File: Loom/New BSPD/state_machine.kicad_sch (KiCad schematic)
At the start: 13 parts, among them U1 4011, U11 4012, U12 74LS573, U3 4011, U4 4011, U5 4011, U6 4011, U7 4011, U8 4011

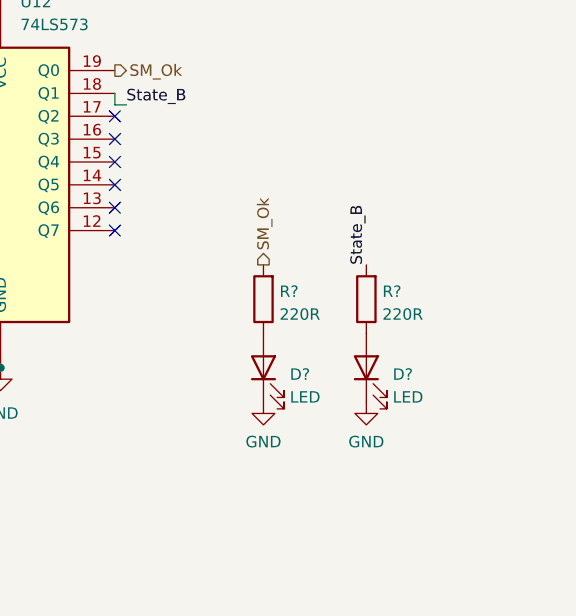
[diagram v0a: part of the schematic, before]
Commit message: Add test points
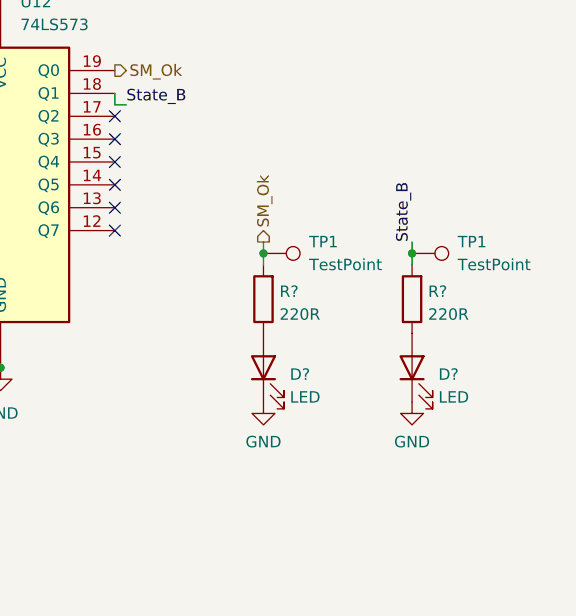
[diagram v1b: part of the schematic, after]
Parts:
- added TP1 (x2): TestPoint, TestPoint:TestPoint_THTPad_D3.0mm_Drill1.5mm, symbol Connector:TestPoint
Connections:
- net SM_Ok: now also TP1.1
- net State_B: now also TP1.1
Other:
- moved on the sheet: D?, R?
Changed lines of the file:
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@@
   (junction (at 171.45 22.86) (diameter 0) (color 0 0 0 0)
   )
+  (junction (at 252.73 71.12) (diameter 0) (color 0 0 0 0)
+  )
   (junction (at 158.75 55.88) (diameter 0) (color 0 0 0 0)
+  )
+  (junction (at 269.24 71.12) (diameter 0) (color 0 0 0 0)
   )
   (junction (at 223.52 83.82) (diameter 0) (color 0 0 0 0)
@@
     (stroke (width 0) (type default))
   )
+  (wire (pts (xy 252.73 71.12) (xy 252.73 72.39))
+    (stroke (width 0) (type default))
+  )
   (wire (pts (xy 109.22 74.93) (xy 113.03 74.93))
     (stroke (width 0) (type default))
@@
     (stroke (width 0) (type default))
   )
+  (wire (pts (xy 269.24 69.85) (xy 269.24 71.12))
+    (stroke (width 0) (type default))
+  )
   (wire (pts (xy 129.54 46.99) (xy 135.89 46.99))
     (stroke (width 0) (type default))
@@
     (stroke (width 0) (type default))
   )
+  (wire (pts (xy 252.73 69.85) (xy 252.73 71.12))
+    (stroke (width 0) (type default))
+  )
   (wire (pts (xy 158.75 30.48) (xy 158.75 43.18))
     (stroke (width 0) (type default))
@@
   )
   (wire (pts (xy 92.71 72.39) (xy 92.71 77.47))
+    (stroke (width 0) (type default))
+  )
+  (wire (pts (xy 269.24 71.12) (xy 269.24 72.39))
     (stroke (width 0) (type default))
   )
@@
     (effects (font (size 1.27 1.27)) (justify right bottom))
   )
-  (label "State_B" (at 264.16 72.39 90) (fields_autoplaced)
+  (label "State_B" (at 269.24 69.85 90) (fields_autoplaced)
     (effects (font (size 1.27 1.27)) (justify left bottom))
   )
@@
     (effects (font (size 1.27 1.27)) (justify right))
   )
-  (hierarchical_label "SM_Ok" (shape output) (at 252.73 72.39 90) (fields_autoplaced)
+  (hierarchical_label "SM_Ok" (shape output) (at 252.73 69.85 90) (fields_autoplaced)
     (effects (font (size 1.27 1.27)) (justify left))
   )
@@
     )
   )
-  (symbol (lib_id "Device:LED") (at 264.16 83.82 90) (unit 1)
-    (in_bom yes) (on_board yes) (dnp no) (fields_autoplaced)
-    (property "Reference" "D?" (at 267.081 84.5728 90)
+  (symbol (lib_id "Device:LED") (at 269.24 83.82 90) (unit 1)
+    (in_bom yes) (on_board yes) (dnp no) (fields_autoplaced)
+    (property "Reference" "D?" (at 272.161 84.5728 90)
       (effects (font (size 1.27 1.27)) (justify right))
     )
-    (property "Value" "LED" (at 267.081 87.1097 90)
+    (property "Value" "LED" (at 272.161 87.1097 90)
       (effects (font (size 1.27 1.27)) (justify right))
     )
-    (property "Footprint" "LED_THT:LED_D5.0mm" (at 264.16 83.82 0)
-      (effects (font (size 1.27 1.27)) hide)
-    )
-    (property "Datasheet" "~" (at 264.16 83.82 0)
+    (property "Footprint" "LED_THT:LED_D5.0mm" (at 269.24 83.82 0)
+      (effects (font (size 1.27 1.27)) hide)
+    )
+    (property "Datasheet" "~" (at 269.24 83.82 0)
       (effects (font (size 1.27 1.27)) hide)
     )
@@
     )
   )
-  (symbol (lib_id "Device:R") (at 264.16 76.2 180) (unit 1)
-    (in_bom yes) (on_board yes) (dnp no) (fields_autoplaced)
-    (property "Reference" "R?" (at 265.938 75.3653 0)
+  (symbol (lib_id "Device:R") (at 269.24 76.2 180) (unit 1)
+    (in_bom yes) (on_board yes) (dnp no) (fields_autoplaced)
+    (property "Reference" "R?" (at 271.018 75.3653 0)
       (effects (font (size 1.27 1.27)) (justify right))
     )
-    (property "Value" "220R" (at 265.938 77.9022 0)
+    (property "Value" "220R" (at 271.018 77.9022 0)
       (effects (font (size 1.27 1.27)) (justify right))
     )
-    (property "Footprint" "Resistor_THT:R_Axial_DIN0207_L6.3mm_D2.5mm_P7.62mm_Horizontal" (at 265.938 76.2 90)
-      (effects (font (size 1.27 1.27)) hide)
-    )
-    (property "Datasheet" "~" (at 264.16 76.2 0)
+    (property "Footprint" "Resistor_THT:R_Axial_DIN0207_L6.3mm_D2.5mm_P7.62mm_Horizontal" (at 271.018 76.2 90)
+      (effects (font (size 1.27 1.27)) hide)
+    )
+    (property "Datasheet" "~" (at 269.24 76.2 0)
       (effects (font (size 1.27 1.27)) hide)
     )
@@
     )
   )
-  (symbol (lib_id "power:GND") (at 264.16 87.63 0) (unit 1)
-    (in_bom yes) (on_board yes) (dnp no) (fields_autoplaced)
-    (property "Reference" "#PWR?" (at 264.16 93.98 0)
-      (effects (font (size 1.27 1.27)) hide)
-    )
-    (property "Value" "GND" (at 264.16 92.0734 0)
-      (effects (font (size 1.27 1.27)))
-    )
-    (property "Footprint" "" (at 264.16 87.63 0)
-      (effects (font (size 1.27 1.27)) hide)
-    )
-    (property "Datasheet" "" (at 264.16 87.63 0)
+  (symbol (lib_id "power:GND") (at 269.24 87.63 0) (unit 1)
+    (in_bom yes) (on_board yes) (dnp no) (fields_autoplaced)
+    (property "Reference" "#PWR?" (at 269.24 93.98 0)
+      (effects (font (size 1.27 1.27)) hide)
+    )
+    (property "Value" "GND" (at 269.24 92.0734 0)
+      (effects (font (size 1.27 1.27)))
+    )
+    (property "Footprint" "" (at 269.24 87.63 0)
+      (effects (font (size 1.27 1.27)) hide)
+    )
+    (property "Datasheet" "" (at 269.24 87.63 0)
       (effects (font (size 1.27 1.27)) hide)
     )
@@
     )
   )
+  (symbol (lib_id "Connector:TestPoint") (at 252.73 71.12 270) (unit 1)
+    (in_bom yes) (on_board yes) (dnp no) (fields_autoplaced)
+    (property "Reference" "TP1" (at 257.81 69.85 90)
+      (effects (font (size 1.27 1.27)) (justify left))
+    )
+    (property "Value" "TestPoint" (at 257.81 72.39 90)
+      (effects (font (size 1.27 1.27)) (justify left))
+    )
+    (property "Footprint" "TestPoint:TestPoint_THTPad_D3.0mm_Drill1.5mm" (at 252.73 76.2 0)
+      (effects (font (size 1.27 1.27)) hide)
+    )
+    (property "Datasheet" "~" (at 252.73 76.2 0)
+      (effects (font (size 1.27 1.27)) hide)
+    )
+    (pin "1")
+    (instances
+      (project "New BSPD"
+        (path "/1f7c501a-057f-4634-92ce-528b01503799"
+          (reference "TP1") (unit 1)
+        )
+        (path "/1f7c501a-057f-4634-92ce-528b01503799/c1af1d02-f1c8-42b8-8d3c-ac3883e05aae"
+          (reference "TP3") (unit 1)
+        )
+      )
+    )
+  )
   (symbol (lib_id "4xxx:4011") (at 86.36 134.62 0) (unit 3)
     (in_bom yes) (on_board yes) (dnp no) (fields_autoplaced)
@@
         )
       )
+    )
+  )
+  (symbol (lib_id "Connector:TestPoint") (at 269.24 71.12 270) (unit 1)
+    (in_bom yes) (on_board yes) (dnp no) (fields_autoplaced)
+    (property "Reference" "TP1" (at 274.32 69.85 90)
+      (effects (font (size 1.27 1.27)) (justify left))
+    )
+    (property "Value" "TestPoint" (at 274.32 72.39 90)
+      (effects (font (size 1.27 1.27)) (justify left))
+    )
+    (property "Footprint" "TestPoint:TestPoint_THTPad_D3.0mm_Drill1.5mm" (at 269.24 76.2 0)
+      (effects (font (size 1.27 1.27)) hide)
+    )
+    (property "Datasheet" "~" (at 269.24 76.2 0)
+      (effects (font (size 1.27 1.27)) hide)
+    )
+    (pin "1")
+    (instances
+      (project "New BSPD"
+        (path "/1f7c501a-057f-4634-92ce-528b01503799"
+          (reference "TP1") (unit 1)
+        )
+        (path "/1f7c501a-057f-4634-92ce-528b01503799/c1af1d02-f1c8-42b8-8d3c-ac3883e05aae"
+          (reference "TP4") (unit 1)
+        )
+      )

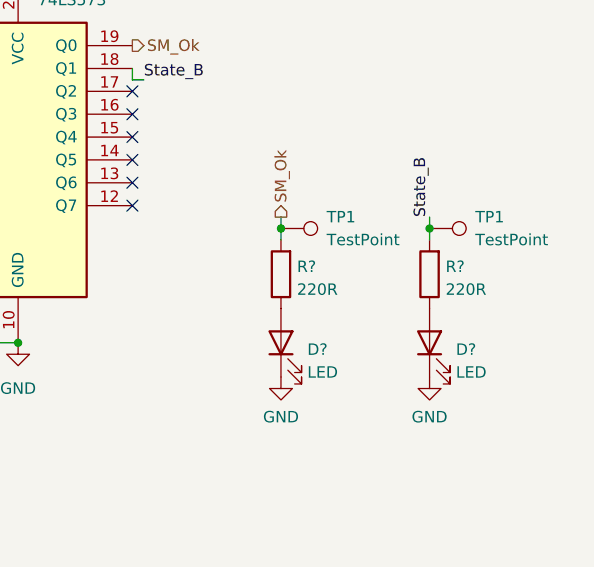
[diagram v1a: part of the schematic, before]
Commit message: Fix BSPD Crystal Footprint
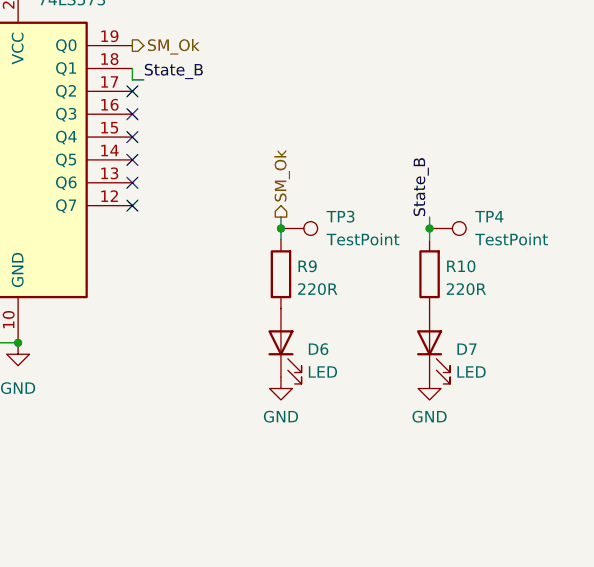
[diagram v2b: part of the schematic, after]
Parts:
- gave numbers to parts that had none: 4
- renumbered TP1 to TP3, TP1 to TP4
